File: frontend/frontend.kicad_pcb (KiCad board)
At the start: 2 copper layers, 32.5 x 22.5 mm, 54 parts, among them Q1 T2N7002AK,LM, Q2 NX3008PBK,215, Q3 NX3008PBK,215, Q4 T2N7002AK,LM, Q5 NX3008PBK,215, Q6 T2N7002AK,LM, U1 ADS1291/2, U2 KC2016Z2

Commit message: Allow reading back CLKSEL
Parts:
- removed R15: 1M, Resistor_SMD:R_0603_1608Metric
- moved C3 0.08 mm to (134.2, 71.6)
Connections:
- U1 pad 25: Net-(U1-GPIO2/RCLK2) -> Net-(JP1-C)
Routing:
- net Net-(JP1-C): track 11.5 -> 24.6 mm, vias 0 -> 2
- net Net-(U1-GPIO2/RCLK2): track 2.82 -> 0.00 mm

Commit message: Update frontend layout
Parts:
- removed C13: 100nF, Capacitor_SMD:C_0603_1608Metric
- removed C14, C15: 1uF, Capacitor_SMD:C_0603_1608Metric
- removed R5: 4.7k, Resistor_SMD:R_0603_1608Metric
- removed R6, R7: 1M, Resistor_SMD:R_0603_1608Metric
- added CLK_EN: ~, frontend_parts:PAD, F.Cu at (141.9, 73.4)
- R12: value 1M -> 47k
- R3: value 1M -> 100k
- R4: value 4.7k -> 1M
- moved R4 23.8 mm to (141.8, 75.7), turned to 90 degrees
- moved JP1 5.23 mm to (134.6, 79.7), turned to 180 degrees
- moved R16 2.63 mm to (139.9, 72.5)
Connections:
- C11 pad 1: Net-(C11-Pad1) -> Net-(U1-IN1N)
- C12 pad 1: Net-(C12-Pad1) -> Net-(U1-IN1P)
- R1 pad 2: Net-(C11-Pad1) -> Net-(U1-IN1N)
- R2 pad 2: Net-(C12-Pad1) -> Net-(U1-IN1P)
- R4 pad 1: Net-(C11-Pad1) -> GND
- R4 pad 2: Net-(C13-Pad1) -> Net-(U2-INH)
- U2 pad 1: Net-(U1-~{PDN}/~{RESET}) -> Net-(U2-INH)
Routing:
- net /VGND: track 13.2 -> 3.26 mm, vias 2 -> 0
- net Net-(U2-INH): track 0.00 -> 9.82 mm, vias 0 -> 1
- net Net-(JP1-C): track 24.6 -> 15.9 mm
- net Net-(U1-IN1P): track 7.94 -> 14.6 mm
- net Net-(U1-IN1N): track 7.19 -> 13.3 mm
- net Net-(C13-Pad2): track 3.14 -> 0.00 mm
- net Net-(C13-Pad1): track 3.08 -> 0.00 mm
- net Net-(C11-Pad1): track 2.95 -> 0.00 mm
- net Net-(C12-Pad1): track 2.95 -> 0.00 mm
- net GNDA: track 8.54 -> 6.79 mm
- net +BATT: track 53.7 -> 52.7 mm
- net Net-(U1-DIN): track 9.30 -> 10.1 mm
- net Net-(U1-~{PDN}/~{RESET}): track 17.0 -> 16.3 mm
- net Net-(U1-DOUT): track 12.2 -> 12.7 mm
- net GND: vias 11 -> 9
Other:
- board text added: "Card/IO module v1r2"
- board text removed: "Card/IO module v1r1"

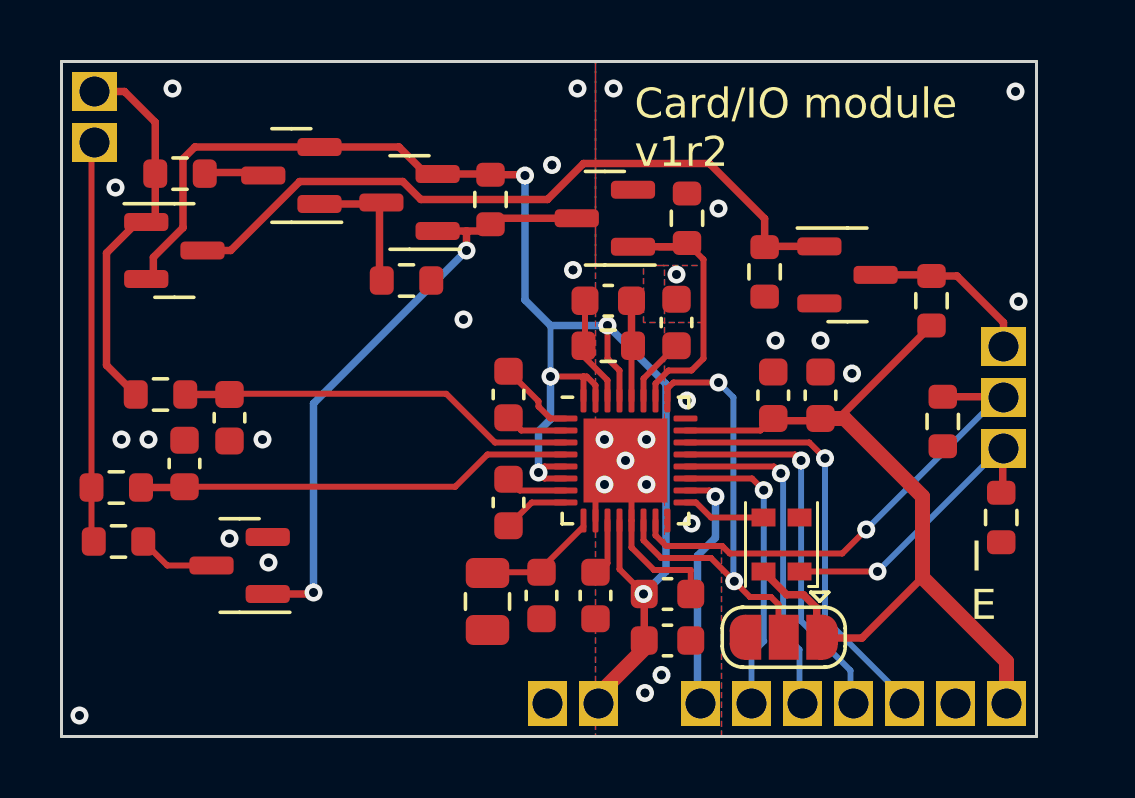
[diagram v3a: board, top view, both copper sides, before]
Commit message: Fix #18: add RLD output, fix main board revision
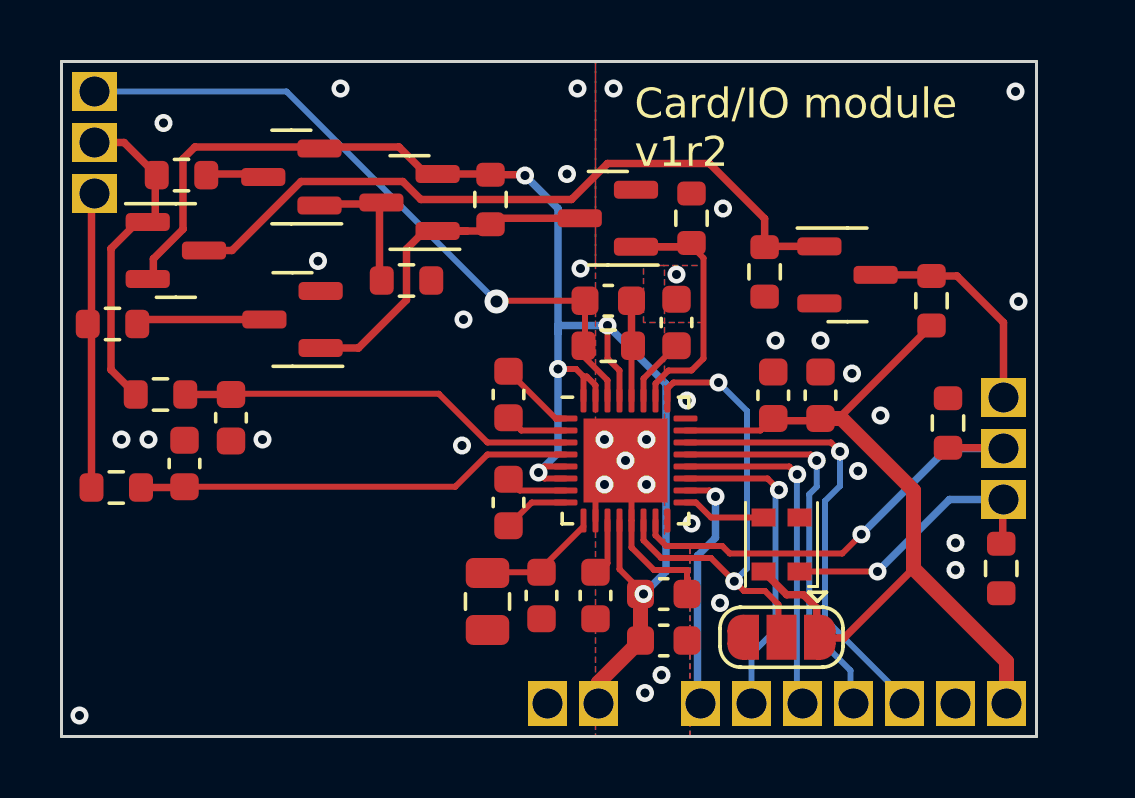
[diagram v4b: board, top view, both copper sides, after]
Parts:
- added RLD_OUT: ~, frontend_parts:PAD, B.Cu at (111.6, 61.5)
- moved Q4 8.39 mm to (118.2, 69.1)
- moved R12 7.25 mm to (112.2, 69.2)
- moved ECG_L1 1.70 mm to (111.6, 63.2)
- moved ECG_R1 1.70 mm to (111.6, 64.9)
- moved R4 1.70 mm to (141.8, 77.4)
- moved ~{RESET}/~{PDN}1 1.70 mm to (141.9, 73.4)
- moved ~{TOUCH_DET}1 1.70 mm to (141.9, 71.7)
- moved CLK_EN 1.70 mm to (141.9, 75.1)
- moved R16 0.18 mm to (140.1, 72.5), turned to -90 degrees
- moved R11 0.15 mm to (131.5, 65.7)
- moved C1 0.12 mm to (130.6, 78.2)
- moved C2 0.12 mm to (130.6, 79.8)
- moved Q1 0.10 mm to (128.7, 65.7)
- moved JP1 0.07 mm to (134.5, 79.7)
- moved R3 0.07 mm to (114.5, 64.3)
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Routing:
- net /VGND: track 3.26 -> 22.5 mm, vias 0 -> 1
- net /TOFF: track 19.9 -> 11.7 mm, vias 2 -> 0
- net Net-(ECG_R1-Pad1): track 12.7 -> 9.84 mm
- net Net-(Q5-G): track 12.8 -> 10.5 mm
- net Net-(Q6-D): track 5.67 -> 7.37 mm
- net Net-(Q4-D): track 2.67 -> 4.35 mm
- net Net-(U1-~{DRDY}): track 13.8 -> 14.7 mm
- net Net-(U1-DIN): track 10.1 -> 10.8 mm
- net Net-(U1-~{PDN}/~{RESET}): track 16.3 -> 15.6 mm
- net Net-(U2-INH): track 9.82 -> 9.22 mm
- net Net-(U1-DOUT): track 12.7 -> 13.2 mm
- net GND: vias 9 -> 14
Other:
- board text removed: "I E"

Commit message: Tweak frontend routing
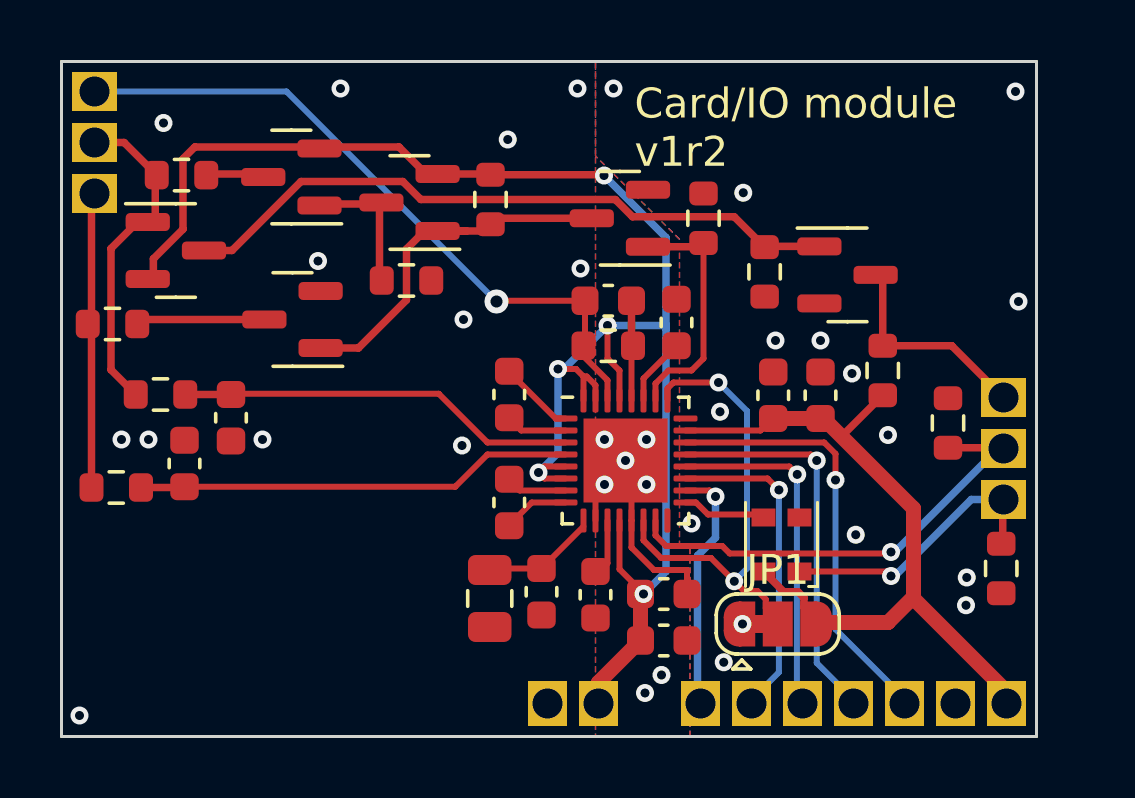
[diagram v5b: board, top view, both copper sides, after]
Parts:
- JP1: footprint Jumper:SolderJumper-3_P1.3mm_Open_RoundedPad1.0x1.5mm -> Jumper:SolderJumper-3_P1.3mm_Bridged12_RoundedPad1.0x1.5mm
- moved R14 2.84 mm to (137.9, 70.8)
- moved JP1 0.46 mm to (134.4, 79.2), turned to 0 degrees
- moved Q1 0.40 mm to (129.1, 65.7)
- moved R11 0.40 mm to (131.9, 65.7)
- moved C10 0.12 mm to (126.5, 78.2)
- moved C9 0.12 mm to (124.8, 78.4)
- renumbered CLK_EN to CLK_EN1, RLD_OUT to RLD_OUT1
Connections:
- JP1 pad 1: +3.3V -> GND
- JP1 pad 3: GND -> +3.3V
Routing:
- net +BATT: track 53.0 -> 56.2 mm
- net Net-(Q5-D): track 23.7 -> 22.2 mm
- net +3.3V: track 28.4 -> 29.3 mm
- net /TOUCH_OFF: track 9.18 -> 8.46 mm
- net Net-(U1-~{DRDY}): track 14.7 -> 14.1 mm
- net GNDA: vias 20 -> 19
- net GND: vias 14 -> 15

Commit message: Add logo to daughter board
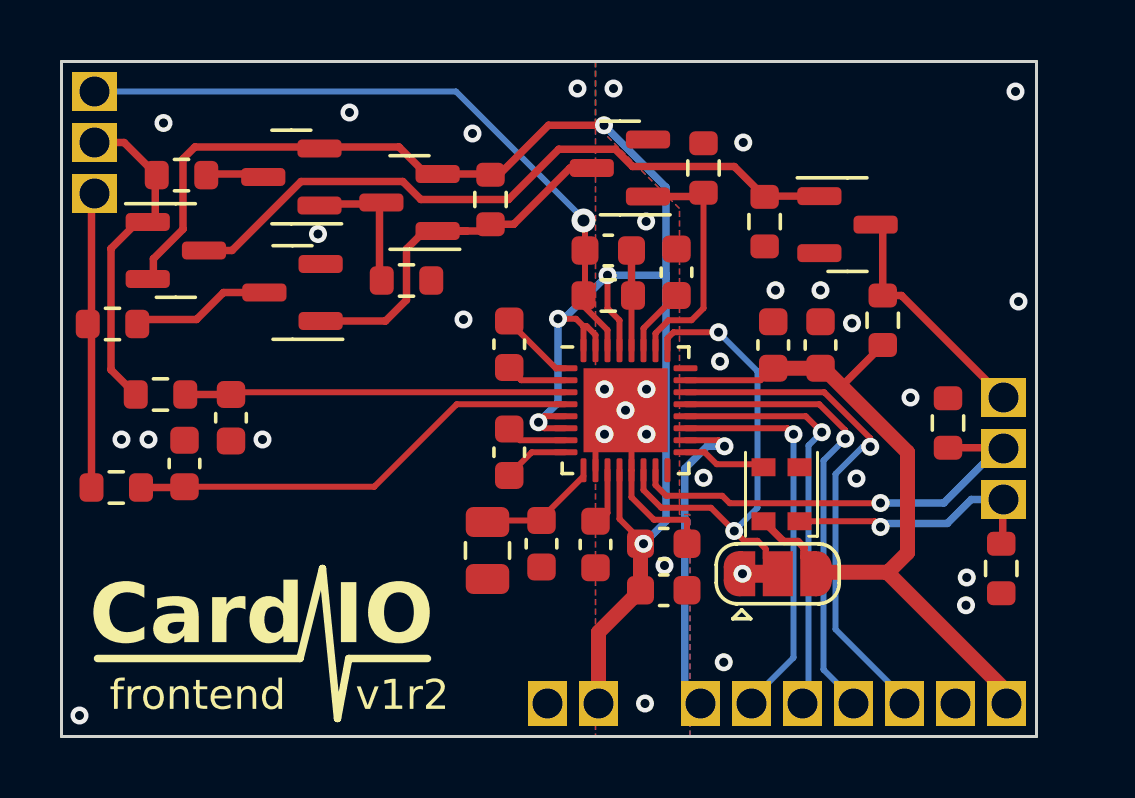
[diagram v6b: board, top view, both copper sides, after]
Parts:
- added G1: ~, frontend_parts:logo, F.Cu at (117.2, 80.4)
- moved C7 1.68 mm to (128.3, 76.6)
- moved C1 1.67 mm to (130.6, 76.6)
- moved C16 1.67 mm to (128.7, 66.8)
- moved C2 1.67 mm to (130.6, 78.1)
- moved C3 1.67 mm to (134.2, 70.0)
- moved C4 1.67 mm to (135.8, 70.0)
- moved C5 1.67 mm to (125.4, 73.5)
- moved C6 1.67 mm to (125.4, 69.9)
- moved C8 1.67 mm to (131.0, 67.5)
- moved JP1 1.67 mm to (134.4, 77.6)
- moved Q1 1.67 mm to (129.1, 64.0)
- moved Q6 1.67 mm to (136.7, 65.9)
- moved R11 1.67 mm to (131.9, 64.0)
- moved R13 1.67 mm to (133.9, 65.8)
- moved R14 1.67 mm to (137.9, 69.1)
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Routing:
- net Net-(U1-~{CS}): track 8.23 -> 11.0 mm
- net Net-(U1-~{DRDY}): track 14.1 -> 16.9 mm
- net Net-(U1-SCLK): track 11.5 -> 14.1 mm
- net +BATT: track 56.2 -> 58.7 mm
- net Net-(U1-DIN): track 10.8 -> 13.2 mm
- net Net-(U1-DOUT): track 13.0 -> 15.5 mm
- net /VGND: track 22.5 -> 24.1 mm
- net /TOFF: track 11.7 -> 12.8 mm
- net Net-(U1-~{PDN}/~{RESET}): track 15.6 -> 14.9 mm
- net Net-(Q5-D): track 22.2 -> 22.9 mm
- net Net-(U1-IN1P): track 14.6 -> 15.3 mm
- net Net-(Q6-D): track 7.20 -> 7.89 mm
- net Net-(U2-INH): track 9.34 -> 8.68 mm
- net Net-(U1-IN1N): track 13.3 -> 12.7 mm
- net GNDA: vias 19 -> 18
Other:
- board text added: "frontend"
- board text added: "v1r2"
- board text removed: "Card/IO module v1r2"

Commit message: Add component values to daugther board
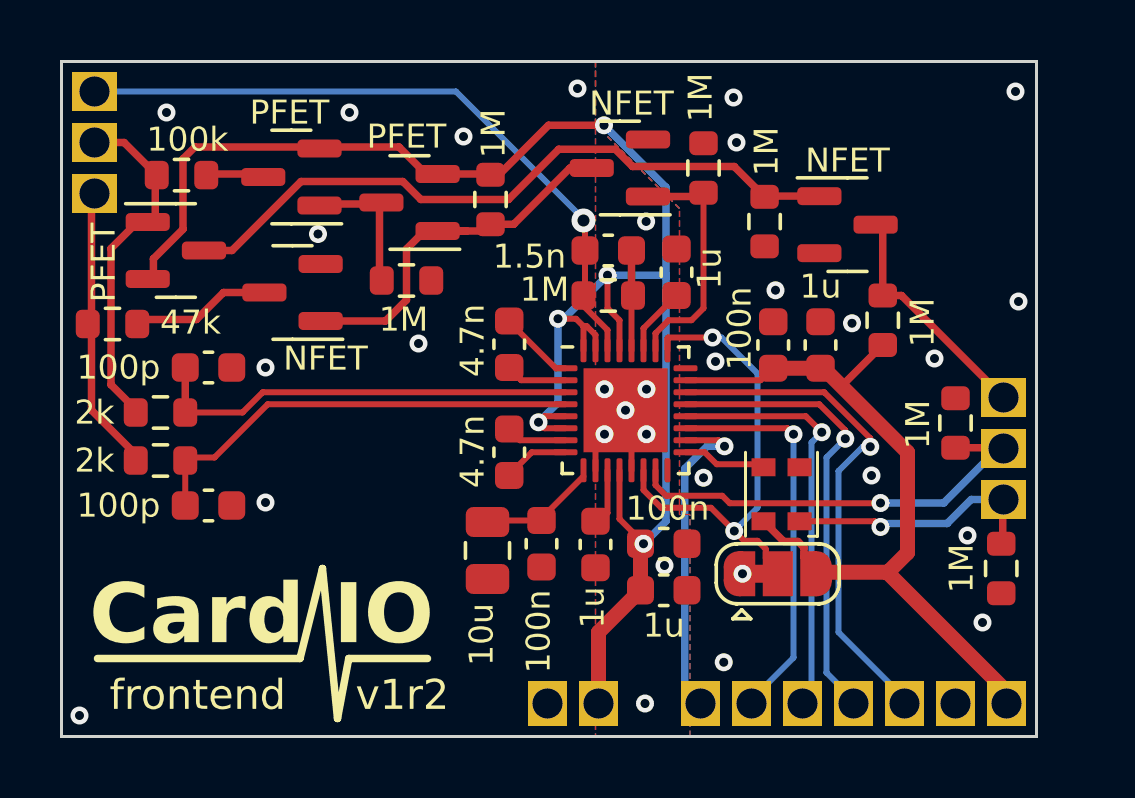
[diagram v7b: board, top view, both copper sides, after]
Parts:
- C1, C10, C3: value 100nF -> 100n
- C11, C12: value 100pF -> 100p
- C16: value 1.5nF -> 1.5n
- C2, C4, C7, C8: value 1uF -> 1u
- C5, C6: value 4.7nF -> 4.7n
- C9: value 10uF -> 10u
- moved C11 1.84 mm to (115.4, 70.7), turned to 0 degrees
- moved R2 1.73 mm to (113.8, 73.8)
- moved C12 1.61 mm to (115.4, 75.3), turned to 0 degrees
- moved R1 0.60 mm to (113.8, 72.2)
- moved R16 0.25 mm to (140.3, 72.5)
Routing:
- net GNDA: track 6.71 -> 2.80 mm, vias 18 -> 17
- net Net-(U1-IN1N): track 12.7 -> 14.5 mm
- net Net-(Q5-G): track 10.5 -> 11.0 mm
- net GND: vias 15 -> 14
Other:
- board text added: "CLK_EN"
- board text added: "RLD_OUT"

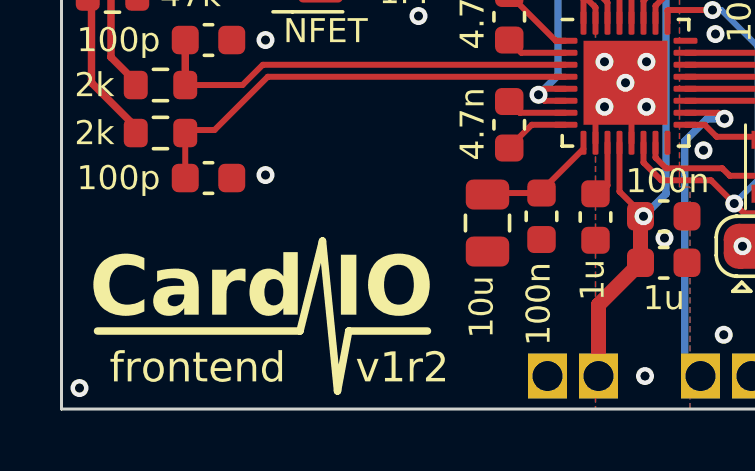
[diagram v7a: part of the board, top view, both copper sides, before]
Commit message: Close #26: add new logo
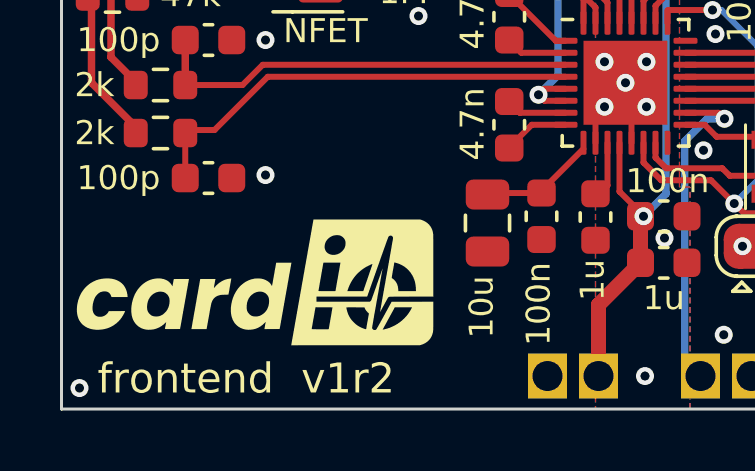
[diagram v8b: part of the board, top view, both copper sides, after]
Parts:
- moved G1 1.32 mm to (118.2, 79.5)
